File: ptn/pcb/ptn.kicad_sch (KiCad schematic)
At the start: 17 parts, among them IC1 GRF5509, J2 142-0701-801

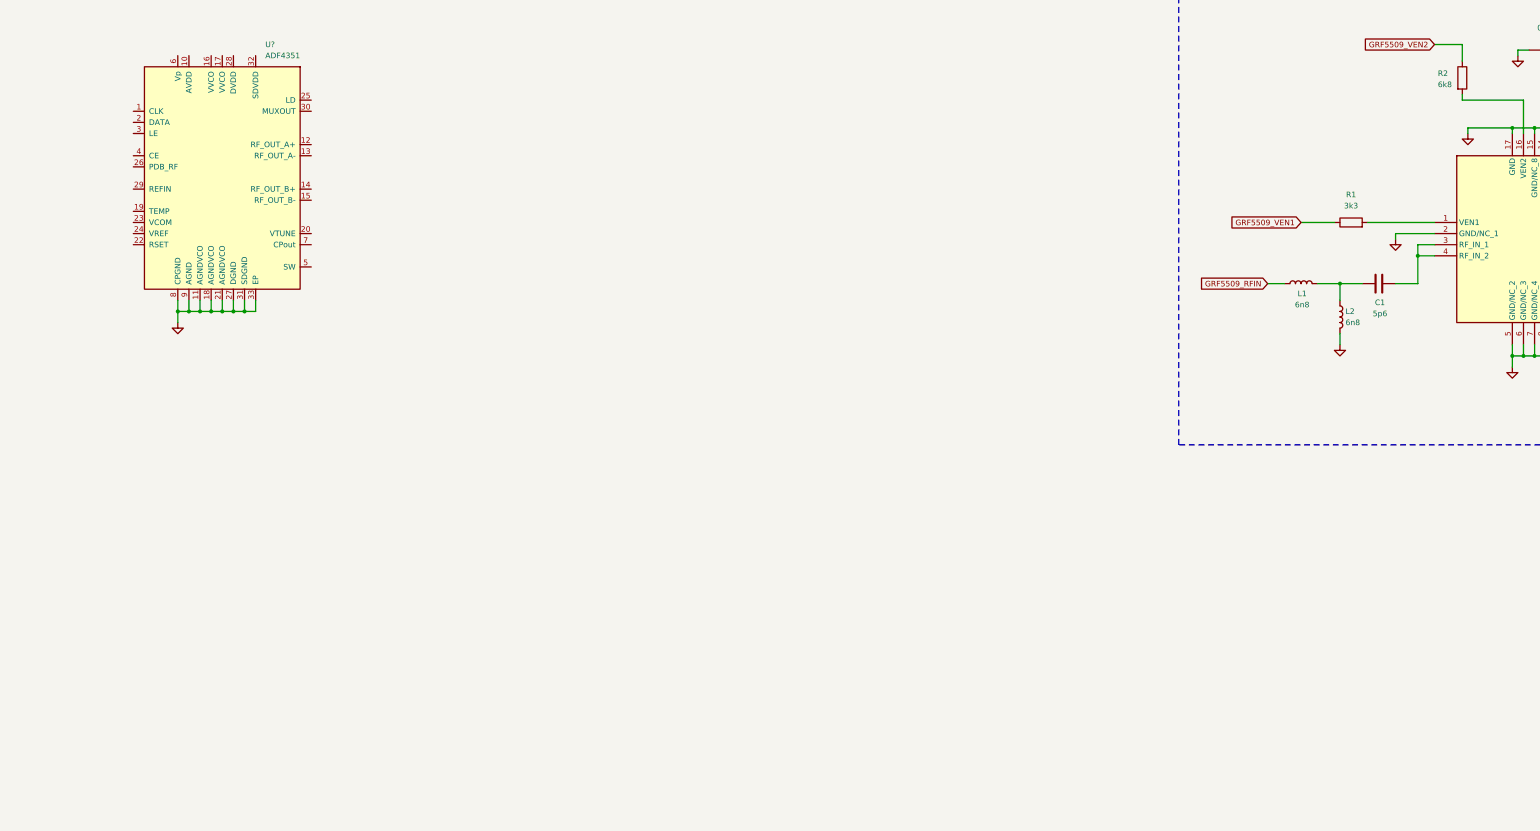
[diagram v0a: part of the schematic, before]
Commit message: Add loop filter
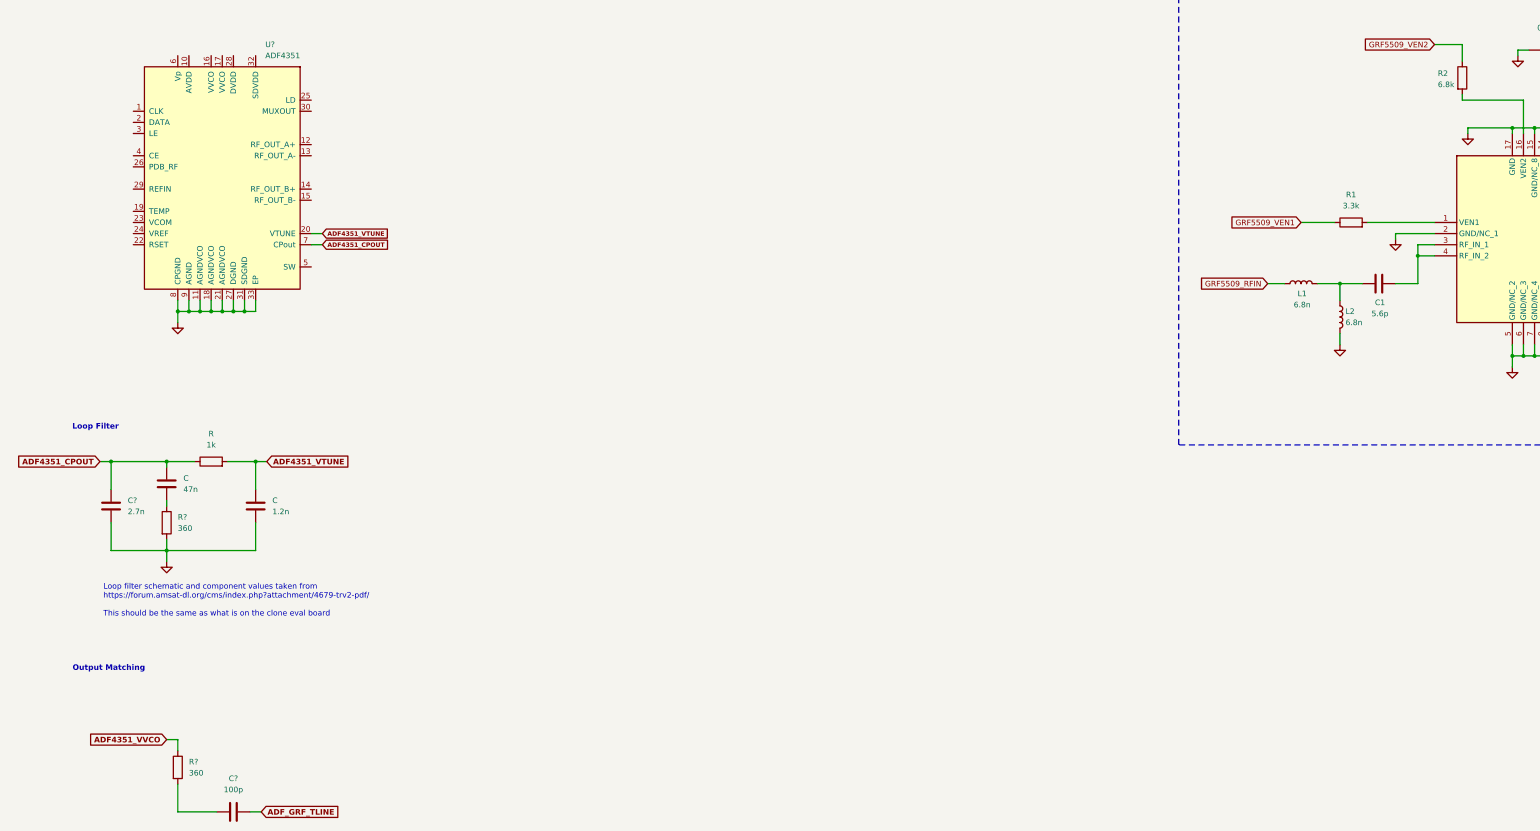
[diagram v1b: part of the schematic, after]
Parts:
- added C: 1.2n, symbol Device:C
- added C: 47n, symbol Device:C
- added C?: 2.7n, symbol Device:C
- added C?: 100p, symbol Device:C
- added R: 1k, symbol Device:R
- added R? (x2): 360, symbol Device:R
- C1: value 5p6 -> 5.6p
- L1, L2: value 6n8 -> 6.8n
- R1: value 3k3 -> 3.3k
- R2: value 6k8 -> 6.8k
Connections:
- net GND: now also C.2, C?.2, R?.2
- net ADF4351_VTUNE: now reaches U?.20 (VTUNE)
- net ADF4351_VTUNE: now also C.1, R.2
- net ADF4351_CPOUT: now reaches U?.7 (CPout)
- net ADF4351_CPOUT: now also C.1, C?.1, R.1
- new net: C.2, R?.1
- new net: C?.1, R?.2
- new net ADF4351_VVCO: R?.1
- new net ADF_GRF_TLINE: C?.2
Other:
- note added: "Loop Filter"
- note added: "Loop filter schematic and component values taken from https://forum.amsat-dl.org/cms/index.php?attachment/4679-trv2-pdf/ This should be the same as what is on the clone eval board"
- note added: "Output Matching"

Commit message: Add decoupling and output matching
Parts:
- added C11, C13, C15, C16, C17, C21, C22, C23, C27: 10p, symbol Device:C
- added C12, C14, C18, C19, C20, C24, C25, C26, C28: 0.1u, symbol Device:C
- added R9: 5.1k, symbol Device:R
- R6: renamed from R?; value 360 -> 50
- gave numbers to parts that had none: 4
- renumbered C to C10, C to C8, R to R8
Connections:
- net GND: now also C11.2, C12.2, C13.2, C14.2, C15.2, C16.2, C17.2, C18.2, C19.2, C20.2, C21.2, C22.2, C23.2, C24.2, C25.2, C26.2, C27.2, C28.2, R9.2
- net ADF4351_RFOUTA+: now reaches C9.1, R6.2
- net ADF4351_RFOUTA+: now also U1.12 (RF_OUT_A+)
- net ADF4351_SCLK: now reaches U1.1 (CLK)
- net +3.3V: now reaches U1.10 (AVDD)
- net +3.3V: now also U1.16 (VVCO), U1.17 (VVCO), U1.28 (DVDD), U1.32 (SDVDD), U1.6 (Vp), C11.1, C12.1, C13.1, C14.1, C16.1, C17.1, C19.1, C20.1, C21.1, C22.1, C24.1, C25.1
- net ADF4351_TEMP: now reaches U1.19 (TEMP)
- net ADF4351_TEMP: now also C15.1, C18.1
- net ADF4351_SDATA: now reaches U1.2 (DATA)
- net at U1.22 (RSET): now also R9.1
- net ADF4351_VCOM: now reaches U1.23 (VCOM)
- net ADF4351_VCOM: now also C23.1, C26.1
- net ADF4351_VREF: now reaches U1.24 (VREF)
- net ADF4351_VREF: now also C27.1, C28.1
- net ADF4351_LD: now reaches U1.25 (LD)
- net ADF4351_PDBRF: now reaches U1.26 (PDB_RF)
- net ADF4351_REFIN: now reaches U1.29 (REFIN)
- net ADF4351_SS: now reaches U1.3 (LE)
- net ADF4351_MUXOUT: now reaches U1.30 (MUXOUT)
- net ADF4351_CE: now reaches U1.4 (CE)
- no-connect marks 0 -> 4
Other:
- note added: "ADF4351"
- note added: "ADF4351 RF Synthesizer"
- note added: "Decoupling"
- note added: "Need to place LDO which converts 5V to 3.3V"
- note added: "Need to place header which breaks out the following signals: 1. 5V 2. GND 3. ADF4351_SCLK 4. ADF4351_MOSI 5. ADF4351_SS 6. ADF4351_CE 7. ADF4351_PDBRF 8. ADF4351_LD 9. ADF4351_MUXOUT"
- note added: "Note: Check SW is needed or not."
- note added: "Other Decoupling:"
- note added: "PLL Loop Filter"
- note added: "Power Supply Decoupling: Place 1x 10pF and 1x 0.1uF capacitor close to each power supply pin (VP, AVDD, VVCO, DVDD, SDVDD) Note: VVCO only needs one pair, even though there are two VVCO pins."
- note added: "Power Supply and IO"
- note added: "RSET resistance taken from same source as loop filter parameters"
- note added: "Reference Input"
- note removed: "Loop Filter"
- moved on the sheet: C1, C10, C2, C3, C4, C5, C6, C7, C8, C9, IC1, J2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

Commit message: Add 3.3V LDO, fix some EDC errors
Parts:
- added C29, C30: 1u, symbol Device:C
- added IC2: ADP150AUJZ-3.3-R7, project_footprint_library:SOT95P280X100-5N, symbol ADP150AUJZ-3_3-R7:ADP150AUJZ-3.3-R7
- added J1: Conn_01x09, symbol Connector_Generic:Conn_01x09
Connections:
- net +3.3V: now also C30.1, IC2.5 (VOUT)
- net +5V: now also C29.1, IC2.1 (VIN), IC2.3 (EN), J1.1 (Pin_1)
- net ADF4351_CE: now also J1.5 (Pin_5)
- net ADF4351_LD: now also J1.7 (Pin_7)
- net ADF4351_MUXOUT: now also J1.8 (Pin_8)
- net ADF4351_PDBRF: now also J1.6 (Pin_6)
- net ADF4351_SCLK: now also J1.2 (Pin_2)
- net GND: now also C29.2, C30.2, IC2.2 (GND), J1.9 (Pin_9)
- net ADF4351_SDATA renamed ADF4351_MOSI
- net ADF4351_MOSI: now also J1.3 (Pin_3)
- net ADF4351_SS renamed ADF4351_SSN
- net ADF4351_SSN: now also J1.4 (Pin_4)
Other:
- note added: "3.3V LDO"
- note added: "IO Header"
- note added: "Need to place header which breaks out the following signals: 1. 5V 2. ADF4351_SCLK 3. ADF4351_MOSI 4. ADF4351_SSN 5. ADF4351_CE 6. ADF4351_PDBRF 7. ADF4351_LD 8. ADF4351_MUXOUT 9. GND"
- note added: "Potentially need to have two of these LDOs to reduce spur contaminated dc feeds"
- note removed: "Need to place LDO which converts 5V to 3.3V"
- note removed: "Need to place header which breaks out the following signals: 1. 5V 2. GND 3. ADF4351_SCLK 4. ADF4351_MOSI 5. ADF4351_SS 6. ADF4351_CE 7. ADF4351_PDBRF 8. ADF4351_LD 9. ADF4351_MUXOUT"

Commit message: Add STM32
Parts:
- added C31, C34, C36, C37, C39: 100n, symbol Device:C
- added C32: 10u, symbol Device:C
- added C33: 10n, symbol Device:C
- added C35, C38: 1u, symbol Device:C
- added C40, C41: 10p, symbol Device:C
- added FB1: 120, symbol Device:FerriteBead
- added J3: Conn_01x04, symbol Connector_Generic:Conn_01x04
- added JP1: BOOT0_SEL, symbol Jumper:Jumper_3_Bridged12
- added R10: 10k, symbol Device:R
- added SW1: SW_Push, symbol Switch:SW_Push
- added U2: STM32F103C8T6, Package_QFP:LQFP-48_7x7mm_P0.5mm, symbol MCU_ST_STM32F1:STM32F103C8Tx
- added Y1: 16MHz, project_footprint_library:16MHz_830108288709, symbol Device:Crystal_GND24
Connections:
- net ADF4351_VVCO is gone; now on net +3.3V: R6.1
- net +3.3V: now also C32.2, C34.2, C36.2, C37.2, C38.2, C39.2, FB1.2, J3.1 (Pin_1), JP1.1 (A), U2.1 (VBAT), U2.24 (VDD), U2.36 (VDD), U2.48 (VDD)
- net +5V: now also R1.1, R2.1
- net ADF4351_CE: now also U2.19 (PB1)
- net ADF4351_LD: now also U2.21 (PB10)
- net ADF4351_MOSI: now also U2.17 (PA7)
- net ADF4351_MUXOUT: now also U2.22 (PB11)
- net ADF4351_PDBRF: now also U2.20 (PB2)
- net ADF4351_SCLK: now also U2.15 (PA5)
- net ADF4351_SSN: now also U2.18 (PB0)
- net GND: now also C31.1, C32.1, C33.1, C34.1, C35.1, C36.1, C37.1, C38.1, C39.1, C40.1, C41.1, J3.4 (Pin_4), JP1.3 (B), SW1.1, U2.23 (VSS), U2.35 (VSS), U2.47 (VSS), U2.8 (VSSA), Y1.2, Y1.4
- net GRF5509_VEN1: now also IC1.1 (VEN1), R1.2; no longer R1.1
- net GRF5509_VEN2: now also IC1.16 (VEN2), R2.2; no longer R2.1
- new net: JP1.2 (C), R10.2
- new net +3.3VA: C33.2, C35.2, FB1.1, U2.9 (VDDA)
- new net STM32_BOOT0: R10.1, U2.44 (BOOT0)
- new net STM32_HSE_IN: C40.2, U2.5 (PD0), Y1.1
- new net STM32_HSE_OUT: C41.2, U2.6 (PD1), Y1.3
- new net STM32_NRST: C31.2, SW1.2, U2.7 (NRST)
- new net SWCLK: J3.2 (Pin_2), U2.37 (PA14)
- new net SWDIO: J3.3 (Pin_3), U2.34 (PA13)
- no-connect marks 4 -> 30
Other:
- note added: "Analog Power Supply Decoupling: --------------------- Place 1x 10nF capacitor very close to VDDA pin Place 1x 1uF capacitor near VDDA pin and FB Place 1x 1uF capacitor near other end of FB"
- note added: "HSE"
- note added: "NRST and BOOT0"
- note added: "Power Supply Decoupling: ----------------- Place 1x 100nF capacitor close to each VDD and VBAT pin Place 1x 10uF capacitor between VDD and GND (only one needed)"
- note added: "Power Supply Decoupling: ---------------------- Place 1x 10pF and 1x 0.1uF capacitor close to each power supply pin (VP, AVDD, VVCO, DVDD, SDVDD) Note: VVCO only needs one pair, even though there are two VVCO pins."
- note added: "STM32F103C8T6"
- note added: "STM32F103C8T6 Microcontroller"
- note added: "SWD"
- note removed: "Power Supply Decoupling: Place 1x 10pF and 1x 0.1uF capacitor close to each power supply pin (VP, AVDD, VVCO, DVDD, SDVDD) Note: VVCO only needs one pair, even though there are two VVCO pins."
- title: (none) -> Power Transmitter Node
- moved on the sheet: C1, C10, C11, C12, C13, C14, C15, C16, C17, C18, C19, C2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

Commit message: Add 12V input and 5V LDO
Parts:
- added C42: 10u, symbol Device:C
- added C43: 22u, symbol Device:C
- added D1: D, project_footprint_library:RF302LAM2STR_DIODE, symbol Device:D
- added IC3: AZ1084CD-5.0TRG1, project_footprint_library:AZ1084CD50TRG1_LDO_5V, symbol AZ1084CD-5_0TRG1_LDO_5V:AZ1084CD-5.0TRG1
- added J4: Barrel_Jack_Switch, project_footprint_library:BARREL_694106301002_1, symbol Connector:Barrel_Jack_Switch
- FB1: value 120 -> 120R
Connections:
- net GND: now also C42.2, C43.2, IC3.1 (GND), J4.2
- new net: C42.1, D1.1 (K), IC3.3 (INPUT)
- new net: D1.2 (A), J4.1
- new net: C43.1, IC3.2 (OUTPUT)
- no-connect marks 30 -> 31
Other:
- note added: "12V Input and 5V LDO"
- moved on the sheet: C29, C30, IC2

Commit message: Add CAN, NRF, and PTN input terminal
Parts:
- removed J1: Conn_01x09, symbol Connector_Generic:Conn_01x09
- removed J4: Barrel_Jack_Switch, project_footprint_library:BARREL_694106301002_1, symbol Connector:Barrel_Jack_Switch
- added D2, D3, D4: LED, symbol Device:LED
- added J1: NRF_CONN, symbol Connector_Generic:Conn_02x04_Counter_Clockwise
- added J4: TB002-500-04BE, project_footprint_library:TB00250004BE_SCREW_TERMINAL, symbol TB002-500-04BE_SCREW_TERMINAL:TB002-500-04BE
- added JP10, JP11, JP2, JP3, JP4, JP5, JP6, JP7, JP8, JP9: Jumper_3_Bridged12, symbol Jumper:Jumper_3_Bridged12
- added R11, R12, R13: 500R, symbol Device:R
- added R14: 1k, symbol Device:R
- added U3: MCP2551-I-SN, Package_SO:SOIC-8_3.9x4.9mm_P1.27mm, symbol Interface_CAN_LIN:MCP2551-I-SN
- R3, R4, R5: value 0 -> 0R
- R6: value 50 -> 50R
- R7: value 360 -> 360R
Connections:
- net ADF_GRF_TLINE is gone; now on net GRF5509_RFIN: C9.2
- net +3.3V: now also J1.4 (Pin_4), R12.2
- net +5V: now also C43.1, IC3.2 (OUTPUT), R11.2, U3.3 (VDD)
- net ADF4351_CE: now also JP8.2 (C); no longer U2.19 (PB1)
- net ADF4351_LD: now also U2.19 (PB1); no longer U2.21 (PB10)
- net ADF4351_MOSI: now also JP4.2 (C); no longer U2.17 (PA7)
- net ADF4351_MUXOUT: now also U2.20 (PB2); no longer U2.22 (PB11)
- net ADF4351_PDBRF: now also JP10.2 (C); no longer U2.20 (PB2)
- net ADF4351_SSN: now also JP6.2 (C); no longer U2.18 (PB0)
- net GND: now also D2.1 (K), D3.1 (K), D4.1 (K), J1.5 (Pin_5), J4.2, R14.1, U3.2 (VSS)
- net at D1.2 (A): now also J4.1
- net STM32_ADF_CE: now reaches U2.13 (PA3)
- net STM32_ADF_CE: now also JP8.1 (A)
- net STM32_SPI1_SSN: now reaches U2.14 (PA4)
- net STM32_SPI1_SSN: now also JP6.1 (A)
- net STM32_SPI1_MISO: now reaches U2.16 (PA6)
- net STM32_USER_LED: now reaches U2.2 (PC13)
- net STM32_USER_LED: now also R13.2
- net STM32_SPI2_SSN: now reaches U2.25 (PB12)
- net STM32_SPI2_SSN: now also JP7.1 (A)
- net STM32_SPI2_SCK: now reaches U2.26 (PB13)
- net STM32_SPI2_SCK: now also JP3.1 (A)
- net STM32_SPI2_MISO: now reaches U2.27 (PB14)
- net STM32_SPI2_MISO: now also JP9.1 (A)
- net STM32_SPI2_MOSI: now reaches U2.28 (PB15)
- net STM32_SPI2_MOSI: now also JP5.1 (A)
- net STM32_NRF_CE: now reaches U2.29 (PA8)
- net STM32_NRF_CE: now also JP11.1 (A)
- net NRF24L01P_IRQ: now reaches U2.30 (PA9)
- net NRF24L01P_IRQ: now also J1.1 (Pin_1)
- net STM32_CANRX: now reaches U2.45 (PB8)
- net STM32_CANRX: now also U3.4 (RXD)
- net STM32_CANTX: now reaches U2.46 (PB9)
- net STM32_CANTX: now also U3.1 (TXD)
- net ADF4351_SCLK renamed ADF4351_SCK
- net ADF4351_SCK: now also JP2.2 (C); no longer U2.15 (PA5)
- new net: D4.2 (A), R13.1
- new net: D3.2 (A), R12.1
- new net: D2.2 (A), R11.1
- new net: R14.2, U3.8 (Rs)
- new net CANH: J4.3, U3.7 (CANH)
- new net CANL: J4.4, U3.6 (CANL)
- new net EXT_ADF_CE: JP8.3 (B)
- new net EXT_ADF_PDBRF: JP10.3 (B)
- new net EXT_NRF_CE: JP11.3 (B)
- new net EXT_SPI1_MOSI: JP4.3 (B)
- new net EXT_SPI1_SCK: JP2.3 (B)
- new net EXT_SPI1_SSN: JP6.3 (B)
- new net EXT_SPI2_MISO: JP9.3 (B)
- new net EXT_SPI2_MOSI: JP5.3 (B)
- new net EXT_SPI2_SCK: JP3.3 (B)
- new net EXT_SPI2_SSN: JP7.3 (B)
- new net NRF24L01P_CE: J1.6 (Pin_6), JP11.2 (C)
- new net NRF24L01P_MISO: J1.8 (Pin_8), JP9.2 (C)
- new net NRF24L01P_MOSI: J1.2 (Pin_2), JP5.2 (C)
- new net NRF24L01P_SCK: J1.7 (Pin_7), JP3.2 (C)
- new net NRF24L01P_SSN: J1.3 (Pin_3), JP7.2 (C)
- new net STM32_ADF_PDBRF: JP10.1 (A), U2.18 (PB0)
- new net STM32_SPI1_MOSI: JP4.1 (A), U2.17 (PA7)
- new net STM32_SPI1_SCK: JP2.1 (A), U2.15 (PA5)
- no-connect marks 31 -> 32
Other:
- note added: "5V LDO"
- note added: "BOOT0"
- note added: "CAN and Wireless"
- note added: "MCP2551 CAN Transceiver"
- note added: "Multiplexing"
- note added: "NRST"
- note added: "PTN Input (12V and CAN)"
- note added: "Power and IO"
- note added: "STM32 Microcontroller"
- note added: "nRF24L01P Header"
- note removed: "12V Input and 5V LDO"
- note removed: "IO Header"
- note removed: "NRST and BOOT0"
- note removed: "Need to place header which breaks out the following signals: 1. 5V 2. ADF4351_SCLK 3. ADF4351_MOSI 4. ADF4351_SSN 5. ADF4351_CE 6. ADF4351_PDBRF 7. ADF4351_LD 8. ADF4351_MUXOUT 9. GND"
- note removed: "Power Supply and IO"
- note removed: "STM32F103C8T6 Microcontroller"
- moved on the sheet: C1, C2, C29, C3, C30, C31, C32, C33, C34, C35, C36, C37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

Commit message: Add second 3V3 LDO, improve IO
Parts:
- removed JP10, JP11, JP2, JP3, JP4, JP5, JP6, JP7, JP8, JP9: Jumper_3_Bridged12, symbol Jumper:Jumper_3_Bridged12
- added C12: 10p, symbol Device:C
- added C14: 0.1u, symbol Device:C
- added C29, C30: 1n, symbol Device:C
- added C3, C9: 1u, symbol Device:C
- added D4: LED, symbol Device:LED
- added IC2: ADP150AUJZ-3.3-R7, project_footprint_library:SOT95P280X100-5N, symbol ADP150AUJZ-3_3-R7:ADP150AUJZ-3.3-R7
- added J2: Conn_02x12_Counter_Clockwise, symbol Connector_Generic:Conn_02x12_Counter_Clockwise
- added JP1, JP10, JP11, JP12, JP2, JP3, JP4, JP5, JP6, JP7, JP8, JP9: Jumper_2_Bridged, symbol Jumper:Jumper_2_Bridged
- added R7: 500R, symbol Device:R
- added R8: 2k, symbol Device:R
- added Y1: SIT5000AICGE-33E0-25.000000X, project_footprint_library:SIT5000AICGE33E025000000X, symbol SIT5000AICGE-33E0-25_000000X:SIT5000AICGE-33E0-25.000000X
- renumbered C7 to C1, C43 to C10, C12 to C13, C13 to C15, C14 to C16, C15 to C17, C16 to C18, C17 to C19, C29 to C2, C18 to C20, C19 to C21, C20 to C22, C21 to C23, C22 to C24, C23 to C25, C24 to C26, C25 to C27, C26 to C28, C27 to C31, C28 to C32, C1 to C33, C2 to C34, C31 to C35, C3 to C36, C32 to C37, C4 to C38, C5 to C39, C8 to C4, C34 to C40, C6 to C41, C36 to C42, C37 to C43, C39 to C44, C33 to C45, C35 to C46, C40 to C47, C38 to C48, C41 to C49, C42 to C5, C9 to C6, C10 to C7, C30 to C8, D4 to D5, IC2 to IC1, IC1 to IC4, J4 to J1, J1 to J3, J2 to J4, J3 to J5, JP1 to JP13, R9 to R1, R14 to R10, R1 to R11, R2 to R12, R3 to R13, R4 to R14, R5 to R15, R10 to R16, R6 to R2, R7 to R3, R8 to R4, R11 to R5, R12 to R6, R13 to R9, Y1 to Y2
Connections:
- net +3.3V: now also J2.2 (Pin_2), J2.23 (Pin_23); no longer C11.1, C13.1, C15.1, C16.1, C18.1, C19.1, C21.1, C22.1, C23.1, C24.1, C26.1, C27.1, R2.1, U1.10 (AVDD), U1.16 (VVCO), U1.17 (VVCO), U1.28 (DVDD), U1.32 (SDVDD), U1.6 (Vp)
- net +3.3VA: now also C11.1, C13.1, C15.1, C16.1, C18.1, C19.1, C21.1, C22.1, C23.1, C24.1, C26.1, C27.1, R2.1, U1.10 (AVDD), U1.16 (VVCO), U1.17 (VVCO), U1.28 (DVDD), U1.32 (SDVDD), U1.6 (Vp), C12.1, C14.1, C9.1, IC2.5 (VOUT), J2.22 (Pin_22), J2.3 (Pin_3), R7.2, R8.1, Y1.4 (VDD); no longer C45.2, C46.2, FB1.1, U2.9 (VDDA)
- net +5V: now also C3.1, IC2.1 (VIN), IC2.3 (EN), J2.1 (Pin_1), J2.24 (Pin_24)
- net ADF4351_CE: now also J2.8 (Pin_8), JP4.2 (B)
- net ADF4351_LD: now also J2.10 (Pin_10)
- net ADF4351_MOSI: now also J2.6 (Pin_6), JP2.2 (B)
- net ADF4351_MUXOUT: now also J2.11 (Pin_11)
- net ADF4351_PDBRF: now also J2.9 (Pin_9), JP5.2 (B)
- net ADF4351_REFIN: now also C30.2
- net ADF4351_SCK: now also J2.5 (Pin_5), JP1.2 (B)
- net ADF4351_SSN: now also J2.7 (Pin_7), JP3.2 (B)
- net GND: now also C12.2, C14.2, C3.2, C9.2, D4.1 (K), IC2.2 (GND), J2.21 (Pin_21), J2.4 (Pin_4), Y1.2 (GND)
- net NRF24L01P_CE: now also J2.16 (Pin_16), JP10.2 (B)
- net NRF24L01P_IRQ: now also J2.15 (Pin_15)
- net NRF24L01P_MISO: now also J2.19 (Pin_19), JP7.2 (B)
- net NRF24L01P_MOSI: now also J2.18 (Pin_18), JP8.2 (B)
- net NRF24L01P_SCK: now also J2.20 (Pin_20), JP6.2 (B)
- net NRF24L01P_SSN: now also J2.17 (Pin_17), JP9.2 (B)
- net STM32_ADF_CE: now also JP4.1 (A)
- net STM32_ADF_PDBRF: now also JP5.1 (A)
- net STM32_CANRX: now also JP12.1 (A)
- net STM32_CANTX: now also JP11.1 (A)
- net STM32_NRF_CE: now also JP10.1 (A)
- net STM32_SPI1_MOSI: now also JP2.1 (A)
- net STM32_SPI1_SCK: now also JP1.1 (A)
- net STM32_SPI1_SSN: now also JP3.1 (A)
- net STM32_SPI2_MISO: now also JP7.1 (A)
- net STM32_SPI2_MOSI: now also JP8.1 (A)
- net STM32_SPI2_SCK: now also JP6.1 (A)
- net STM32_SPI2_SSN: now also JP9.1 (A)
- net 12V_IN: now reaches D1.2 (A), J1.1
- net STM32_ADC1_IN0: now reaches U2.10 (PA0)
- net STM32_ADC1_IN0: now also J2.12 (Pin_12)
- new net: R8.2, Y1.1 (OE)
- new net: D4.2 (A), R7.1
- new net: C29.1, Y1.3 (OUT)
- new net: C29.2, C30.1
- new net MCP2551_CANRX: J2.13 (Pin_13), JP12.2 (B)
- new net MCP2551_CANTX: J2.14 (Pin_14), JP11.2 (B)
- new net VDDA: C45.2, C46.2, FB1.1, U2.9 (VDDA)
- no-connect marks 32 -> 21
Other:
- note added: "3.3V LDOs"
- note added: "IO"
- note added: "Place 10pF and 0.1uF decoupling capacitors close to VDD and GND"
- note added: "Reference 25MHz Input"
- note added: "Try with 7.5nH or more for better matching"
- note removed: "3.3V LDO"
- note removed: "Multiplexing"
- note removed: "Potentially need to have two of these LDOs to reduce spur contaminated dc feeds"
- note removed: "Reference Input"
- moved on the sheet: C2, C35, C37, C40, C41, C42, C43, C44, C45, C46, C47, C48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

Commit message: Add new LDO for non-PLL 3V3
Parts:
- removed C2: 1u, symbol Device:C
- removed D4: LED, symbol Device:LED
- removed IC1: ADP150AUJZ-3.3-R7, project_footprint_library:SOT95P280X100-5N, symbol ADP150AUJZ-3_3-R7:ADP150AUJZ-3.3-R7
- removed R7: 500R, symbol Device:R
- added C1: 10u, symbol Device:C
- added U1: NCP1117-3.3_SOT223, Package_TO_SOT_SMD:SOT-223-3_TabPin2, symbol Regulator_Linear:NCP1117-3.3_SOT223
- C8: value 1u -> 10u
- renumbered C3 to C2, C1 to C3, D5 to D4, IC2 to IC1, IC3 to IC2, IC4 to IC3, R11 to R10, R12 to R11, R13 to R12, R14 to R13, R15 to R14, R16 to R15, R8 to R7, R9 to R8, R10 to R9, U1 to U2, U2 to U3, U3 to U4
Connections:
- net +3.3V: now also U1.2 (VO)
- net +5V: now also C1.1, U1.3 (VI)
- net GND: now also C1.2, U1.1 (GND)
- net +12V: now reaches C5.1, D1.1 (K), IC2.3 (INPUT)
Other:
- moved on the sheet: C2, C9, D1, IC1
